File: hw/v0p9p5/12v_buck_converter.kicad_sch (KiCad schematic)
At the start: 19 parts

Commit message: Updates - candidate board layout
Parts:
- C15, C16: value (none) -> 4.7u; footprint (none) -> Capacitor_SMD:C_0805_2012Metric
- C17, C20: value (none) -> 4.7n; footprint (none) -> Capacitor_SMD:C_0805_2012Metric
- C18: value (none) -> 100n; footprint (none) -> Capacitor_SMD:C_0805_2012Metric
- C19: value (none) -> 10n; footprint (none) -> Capacitor_SMD:C_0805_2012Metric
- C21, C23: value (none) -> 33u; footprint (none) -> Capacitor_SMD:C_0805_2012Metric
- C22: value (none) -> 39p; footprint (none) -> Capacitor_SMD:C_0805_2012Metric
- D8: value (none) -> B340A; footprint (none) -> Diode_SMD:D_SMA
- J9: value (none) -> Test Points; footprint (none) -> Connector_PinHeader_2.54mm:PinHeader_1x03_P2.54mm_Vertical
- L1: value (none) -> 6.8uH; footprint (none) -> raspberrypi_supercap_ups_lib:Sunltech_SLO0530H
- R21: value (none) -> 332k; footprint (none) -> Resistor_SMD:R_0805_2012Metric
- R22: value (none) -> 68.1k; footprint (none) -> Resistor_SMD:R_0805_2012Metric
- R23: value (none) -> 49.9k; footprint (none) -> Resistor_SMD:R_0805_2012Metric
- R24: value (none) -> 0; footprint (none) -> Resistor_SMD:R_0805_2012Metric
- R25: value (none) -> 10.2k; footprint (none) -> Resistor_SMD:R_0805_2012Metric
- R26: value (none) -> 2k; footprint (none) -> Resistor_SMD:R_0805_2012Metric
- U8: value (none) -> TPS54331DR; footprint (none) -> raspberrypi_supercap_ups_lib:SOIC127P599X175-8N

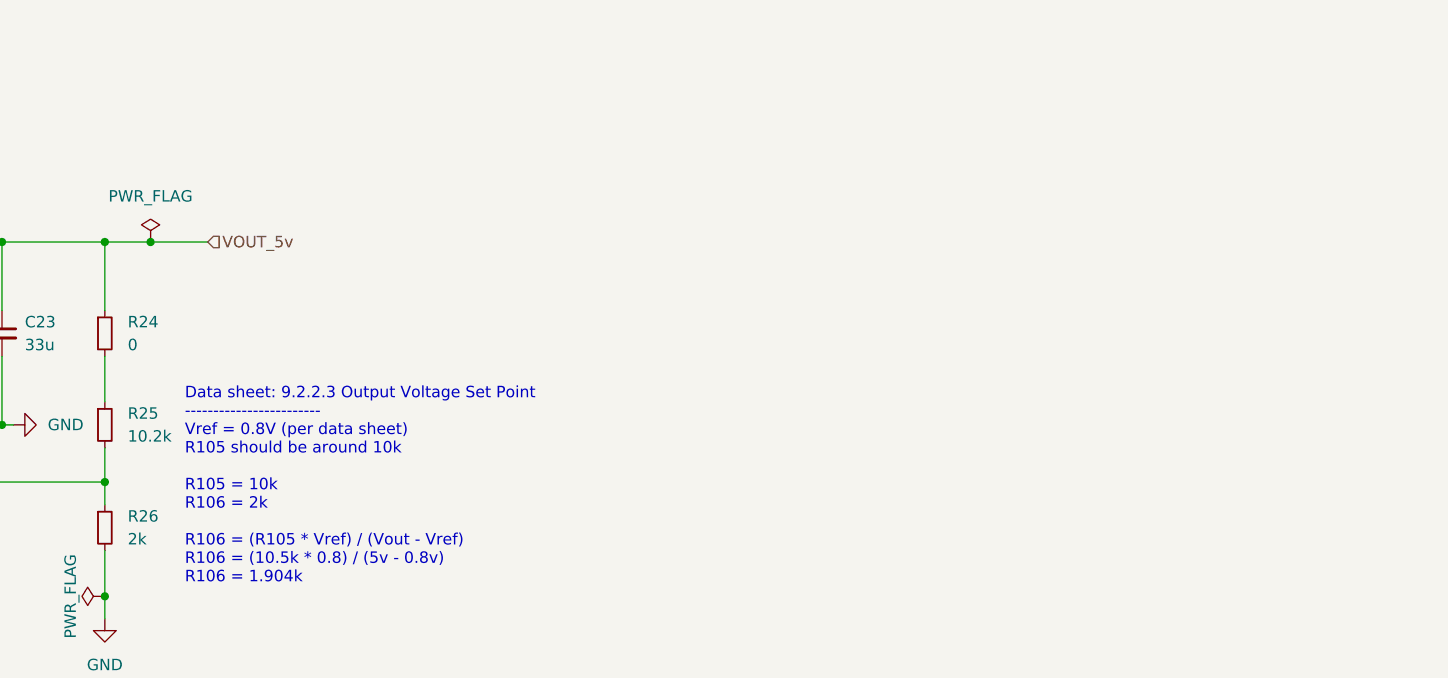
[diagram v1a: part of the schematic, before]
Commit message: Added note about R26
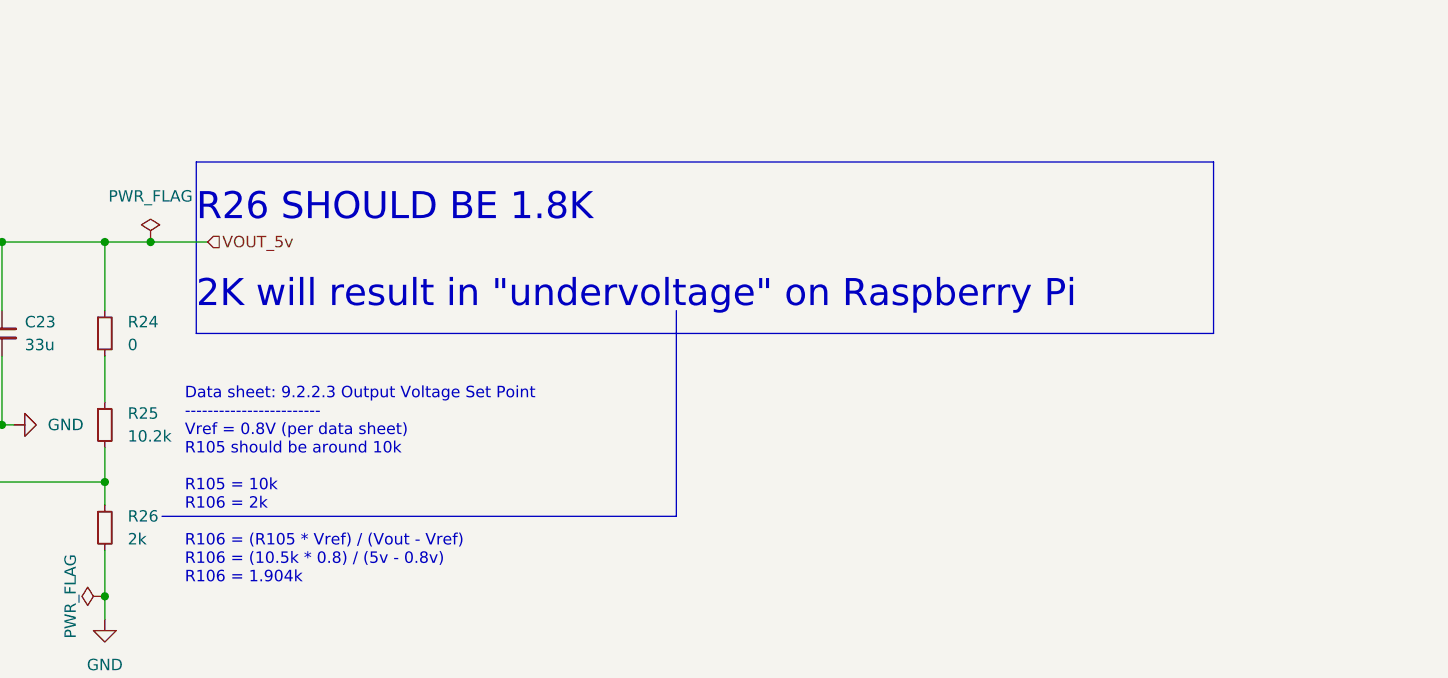
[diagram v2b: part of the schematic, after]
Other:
- note added: "R26 SHOULD BE 1.8K 2K will result in "undervoltage" on Raspberry Pi"
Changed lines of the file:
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@@
   (junction (at 129.54 153.67) (diameter 0) (color 0 0 0 0)
   )
+  (polyline (pts (xy 279.4 125.73) (xy 279.4 106.68))
+    (stroke (width 0) (type default) (color 0 0 0 0))
+  )
   (wire (pts (xy 121.92 115.57) (xy 121.92 121.92))
     (stroke (width 0) (type default) (color 0 0 0 0))
@@
     (stroke (width 0) (type default) (color 0 0 0 0))
   )
+  (polyline (pts (xy 166.37 106.68) (xy 279.4 106.68))
+    (stroke (width 0) (type default) (color 0 0 0 0))
+  )
   (wire (pts (xy 134.62 135.89) (xy 144.78 135.89))
     (stroke (width 0) (type default) (color 0 0 0 0))
@@
     (stroke (width 0) (type default) (color 0 0 0 0))
   )
+  (polyline (pts (xy 166.37 125.73) (xy 279.4 125.73))
+    (stroke (width 0) (type default) (color 0 0 0 0))
+  )
   (wire (pts (xy 156.21 154.94) (xy 156.21 157.48))
     (stroke (width 0) (type default) (color 0 0 0 0))
@@
     (stroke (width 0) (type default) (color 0 0 0 0))
   )
+  (polyline (pts (xy 219.71 123.19) (xy 219.71 146.05))
+    (stroke (width 0) (type default) (color 0 0 0 0))
+  )
   (wire (pts (xy 116.84 132.08) (xy 116.84 115.57))
     (stroke (width 0) (type default) (color 0 0 0 0))
@@
     (stroke (width 0) (type default) (color 0 0 0 0))
   )
+  (polyline (pts (xy 162.56 146.05) (xy 219.71 146.05))
+    (stroke (width 0) (type default) (color 0 0 0 0))
+  )
   (wire (pts (xy 134.62 153.67) (xy 134.62 149.86))
     (stroke (width 0) (type default) (color 0 0 0 0))
@@
     (stroke (width 0) (type default) (color 0 0 0 0))
   )
+  (polyline (pts (xy 166.37 106.68) (xy 166.37 125.73))
+    (stroke (width 0) (type default) (color 0 0 0 0))
+  )
   (wire (pts (xy 73.66 135.89) (xy 85.09 135.89))
     (stroke (width 0) (type default) (color 0 0 0 0))
   )
+  (text "R26 SHOULD BE 1.8K\n\n2K will result in \"undervoltage\" on Raspberry Pi"
+    (at 166.37 123.19 0)
+    (effects (font (size 3 3)) (justify left bottom))
+  )
   (text "Data sheet: 9.2.2.3 Output Voltage Set Point\n------------------------\nVref = 0.8V (per data sheet)\nR105 should be around 10k\n\nR105 = 10k\nR106 = 2k\n\nR106 = (R105 * Vref) / (Vout - Vref)\nR106 = (10.5k * 0.8) / (5v - 0.8v)\nR106 = 1.904k\n"
